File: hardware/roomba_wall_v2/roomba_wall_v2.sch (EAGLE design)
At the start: 13 parts, among them IC1 ATTINY85-20PU, T1 2N2222

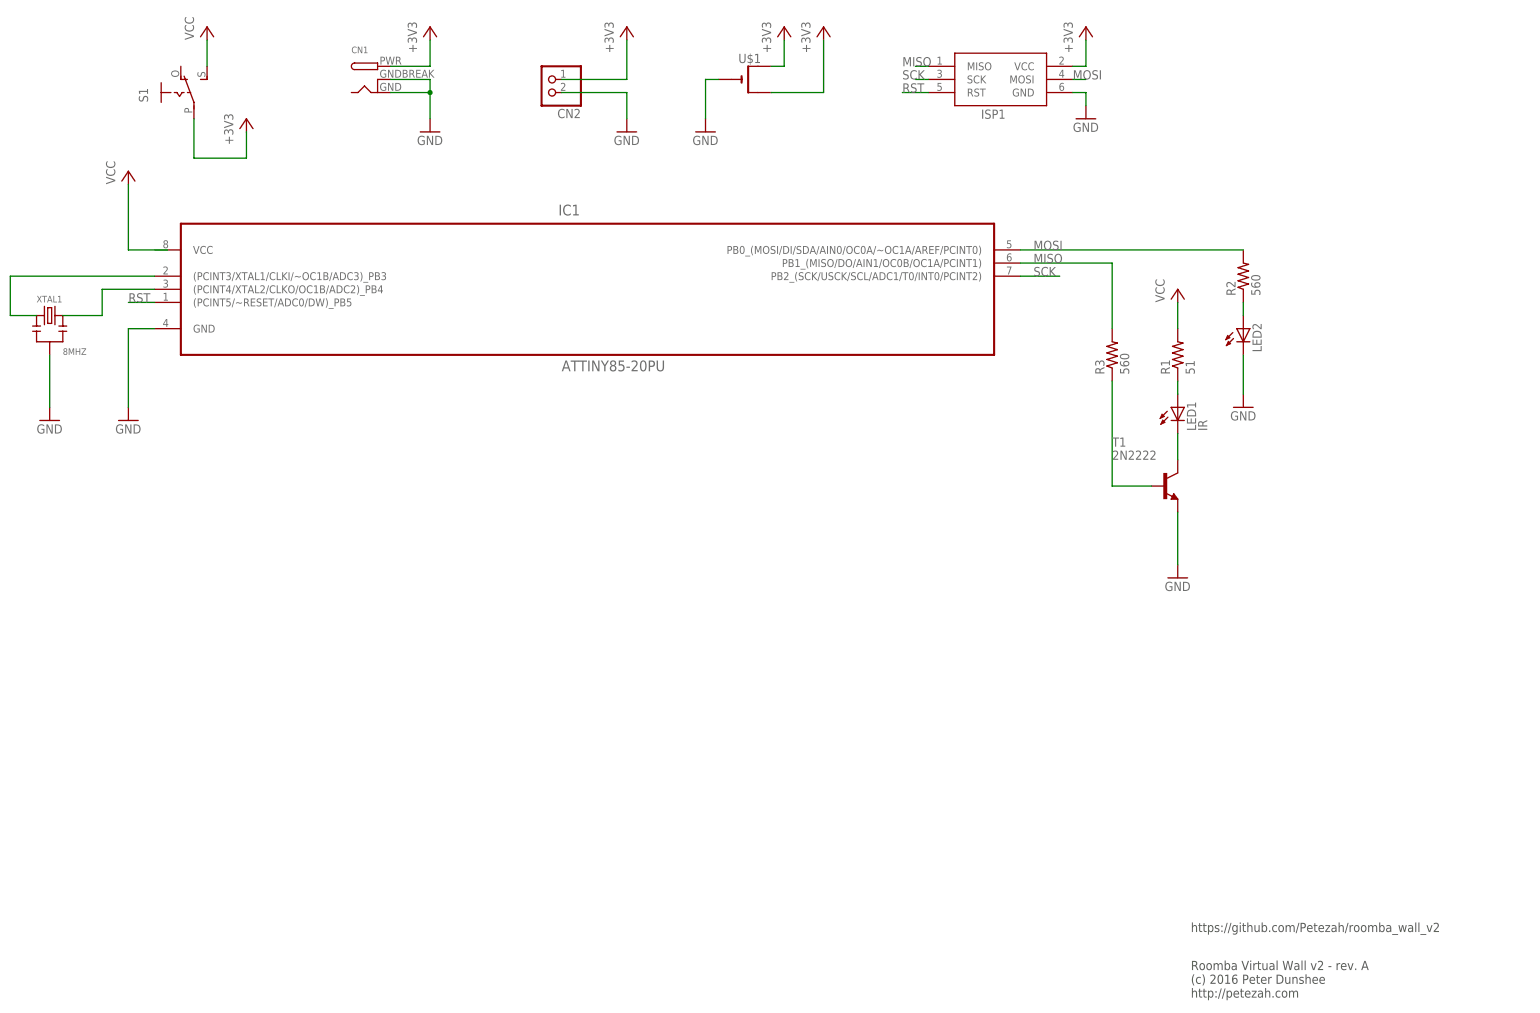
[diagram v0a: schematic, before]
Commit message: PCB layout, rev B 1/3 smaller, with mounting holes and cutout for the battery holder
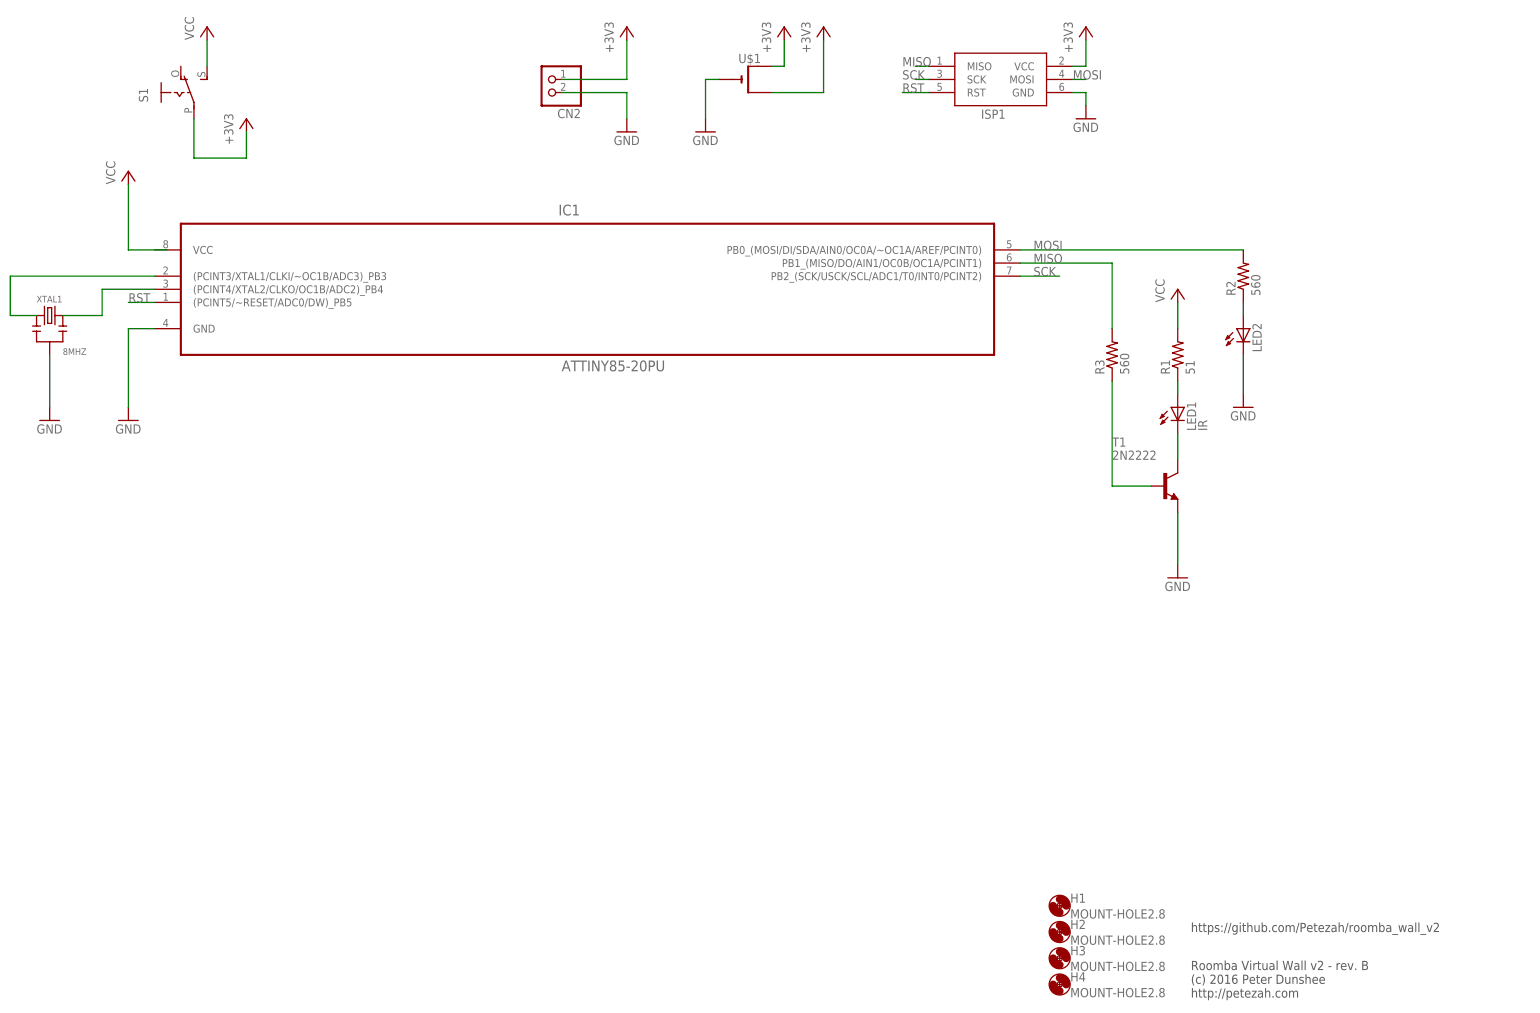
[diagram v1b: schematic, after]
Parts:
- removed CN1: (no value), adafruit:DCBARRELPTH
- added H1, H2, H3, H4: MOUNT-HOLE2.8, holes:MOUNT-HOLE2.8
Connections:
- net +3V3: no longer CN1.PWR
- net GND: no longer CN1.GND, CN1.GNDBREAK
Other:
- note added: "Roomba Virtual Wall v2 - rev. B (c) 2016 Peter Dunshee http://petezah.com"
- note removed: "Roomba Virtual Wall v2 - rev. A (c) 2016 Peter Dunshee http://petezah.com"
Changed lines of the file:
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@@
 <?xml version="1.0" encoding="utf-8"?>
 <!DOCTYPE eagle SYSTEM "eagle.dtd">
-<eagle version="7.5.0">
+<eagle version="7.6.0">
 <drawing>
 <settings>
@@
 <part name="P+2" library="supply1" deviceset="VCC" device=""/>
 <part name="T1" library="adafruit" deviceset="2N2222" device=""/>
-<part name="CN1" library="adafruit" deviceset="DCBARREL" device="PTH"/>
 <part name="R1" library="adafruit" deviceset="R-US_" device="0204/7" value="51"/>
 <part name="R2" library="adafruit" deviceset="R-US_" device="0204/7" value="560"/>
@@
 <part name="P+3" library="supply1" deviceset="VCC" device=""/>
 <part name="U$1" library="adafruit" deviceset="CR2032" device="THM"/>
-<part name="+3V3" library="supply1" deviceset="+3V3" device=""/>
 <part name="+3V4" library="supply1" deviceset="+3V3" device=""/>
 <part name="+3V5" library="supply1" deviceset="+3V3" device=""/>
@@
 <part name="GND6" library="supply1" deviceset="GND" device=""/>
 <part name="GND7" library="supply1" deviceset="GND" device=""/>
-<part name="GND8" library="supply1" deviceset="GND" device=""/>
+<part name="H1" library="holes" deviceset="MOUNT-HOLE" device="2.8"/>
+<part name="H2" library="holes" deviceset="MOUNT-HOLE" device="2.8"/>
+<part name="H3" library="holes" deviceset="MOUNT-HOLE" device="2.8"/>
+<part name="H4" library="holes" deviceset="MOUNT-HOLE" device="2.8"/>
 </parts>
 <sheets>
 <sheet>
 <plain>
-<text x="269.24" y="0" size="1.778" layer="97">Roomba Virtual Wall v2 - rev. A
+<text x="269.24" y="0" size="1.778" layer="97">Roomba Virtual Wall v2 - rev. B
 (c) 2016 Peter Dunshee
 http://petezah.com
@@
 <instance part="P+2" gate="VCC" x="78.74" y="187.96"/>
 <instance part="T1" gate="G$1" x="264.16" y="99.06"/>
-<instance part="CN1" gate="G$1" x="111.76" y="177.8"/>
 <instance part="R1" gate="G$1" x="266.7" y="124.46" rot="R90"/>
 <instance part="R2" gate="G$1" x="279.4" y="139.7" rot="R90"/>
@@
 <instance part="P+3" gate="VCC" x="266.7" y="137.16"/>
 <instance part="U$1" gate="G$1" x="182.88" y="177.8"/>
-<instance part="+3V3" gate="G$1" x="121.92" y="187.96"/>
 <instance part="+3V4" gate="G$1" x="160.02" y="187.96"/>
 <instance part="+3V5" gate="G$1" x="190.5" y="187.96"/>
@@
 <instance part="GND6" gate="1" x="160.02" y="167.64"/>
 <instance part="GND7" gate="1" x="175.26" y="167.64"/>
-<instance part="GND8" gate="1" x="121.92" y="167.64"/>
+<instance part="H1" gate="G$1" x="243.84" y="17.78"/>
+<instance part="H2" gate="G$1" x="243.84" y="12.7"/>
+<instance part="H3" gate="G$1" x="243.84" y="7.62"/>
+<instance part="H4" gate="G$1" x="243.84" y="2.54"/>
 </instances>
 <busses>
@@
 </segment>
 <segment>
-<pinref part="CN1" gate="G$1" pin="GND"/>
-<pinref part="GND8" gate="1" pin="GND"/>
-<wire x1="114.3" y1="175.26" x2="121.92" y2="175.26" width="0.1524" layer="91"/>
-<wire x1="121.92" y1="175.26" x2="121.92" y2="170.18" width="0.1524" layer="91"/>
-<pinref part="CN1" gate="G$1" pin="GNDBREAK"/>
-<wire x1="114.3" y1="177.8" x2="121.92" y2="177.8" width="0.1524" layer="91"/>
-<wire x1="121.92" y1="177.8" x2="121.92" y2="175.26" width="0.1524" layer="91"/>
-<junction x="121.92" y="175.26"/>
-</segment>
-<segment>
 <pinref part="CN2" gate="G$1" pin="1"/>
 <wire x1="147.32" y1="175.26" x2="160.02" y2="175.26" width="0.1524" layer="91"/>
@@
 </segment>
 <segment>
-<pinref part="CN1" gate="G$1" pin="PWR"/>
-<pinref part="+3V3" gate="G$1" pin="+3V3"/>
-<wire x1="114.3" y1="180.34" x2="121.92" y2="180.34" width="0.1524" layer="91"/>
-<wire x1="121.92" y1="180.34" x2="121.92" y2="185.42" width="0.1524" layer="91"/>
-</segment>
-<segment>
